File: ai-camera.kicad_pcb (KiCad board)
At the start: 4 copper layers, 70 x 70 mm, 161 parts, among them J1 Conn-01x02_P2mm_NONAME_JST-PH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, J2 USB_B_Micro_10118194-0001LF, J3 DBG, J4 Conn-02x10_P2.54mm_B-2100S20P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, J5 Conn-01x02_P1.25mm_10114829-1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, J6 Conn_01x24_FFC_0.5mm_hirose_F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, Q1 AO3401A, Q2 AO3400A, Q3 AO3400A, Q4 AO3401A, Q5 AO3400A, Q6 AO3401A, Q7 AO3400A, Q8 AO3400A, SW1 SW_PB_90deg_K2-1102AQ-H4CW-01, SW2 SW_PB_TS-1187A-B-A-B, SW3 SW_PB_TS-1187A-B-A-B, SW4 SW_PB_90deg_K2-1102AQ-H4CW-01, U1 SRV05-4, U10 AP1511B, U11 ESP32-S3-WROOM-1-N16R8, U12 MT9284-28J, U13 APDS-9306-065, U2 TP4057-42-SOT26-R, U3 PCF8563T/5,518, U4 XC6206-2.8V, U5 PIR_BS612, U6 SY8089AAAC, U7 SOT-23-6_SN74LVC1G373DBVR_TI, U8 XC6206-2.8V, U9 RT9166-12GVL, Y1 32.768kHz_Q13FC1350000400

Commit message: EAC-2: begin layout: low impedance ground connections, move DC-DC farther away, USB-C to prevent dips
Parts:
- removed the C29 at (136.8, 80.4)
- removed the C34 at (143.4, 73.1)
- removed the C35 at (141.8, 73.1)
- removed the D1 at (102.8, 87.7)
- removed the D2 at (102.8, 90.1)
- removed the R14 at (103.5, 67.1)
- removed the R17 at (108.3, 67.2)
- removed the R30 at (114.3, 85.7)
- removed RV1, RV2: 1M_3362P-1-105, 00-kiml-potentiometer-tht:Potentiometer_Vishay_T73YP_Vertical
- removed the TP29 at (104.6, 88.7)
- removed the U5 at (105.0, 59.0)
- added C11: 100u_CASE-B-3528_TAJB107K006RNJ, 00-kiml-capacitor-tantalum:CP_EIA-3528-15_AVX-H, F.Cu at (116.7, 101.2)
- added C14: 1u_0603_CL10A105KB8NNNC, Capacitor_SMD:C_0603_1608Metric, F.Cu at (120.9, 103.2)
- added C15: 100n_0402_CL05B104KB54PNC, Capacitor_SMD:C_0402_1005Metric, F.Cu at (119.7, 103.8)
- added C18: 100n_0402_CL05B104KB54PNC, Capacitor_SMD:C_0402_1005Metric, F.Cu at (119.7, 106.2)
- added C19: 10u_0603_CL10A106KP8NNNC, Capacitor_SMD:C_0603_1608Metric, F.Cu at (120.9, 106.8)
- added C21: 10u_0603_CL10A106KP8NNNC, Capacitor_SMD:C_0603_1608Metric, F.Cu at (124.0, 106.8)
- added C25: 10u_0603_CL10A106KP8NNNC, Capacitor_SMD:C_0603_1608Metric, F.Cu at (125.6, 106.8)
- added C27: 10u_0603_CL10A106KP8NNNC, Capacitor_SMD:C_0603_1608Metric, B.Cu at (119.3, 90.4)
- added C3: 1u_0603_CL10A105KB8NNNC, Capacitor_SMD:C_0603_1608Metric, F.Cu at (104.8, 87.0)
- added C31: 10u_0603_CL10A106KP8NNNC, Capacitor_SMD:C_0603_1608Metric, B.Cu at (126.7, 93.7)
- added C37: 100u_CASE-B-3528_TAJB107K006RNJ, 00-kiml-capacitor-tantalum:CP_EIA-3528-15_AVX-H, B.Cu at (152.8, 104.2)
- added C38: 100u_CASE-B-3528_TAJB107K006RNJ, 00-kiml-capacitor-tantalum:CP_EIA-3528-15_AVX-H, B.Cu at (152.8, 107.6)
- added C39: 100u_CASE-B-3528_TAJB107K006RNJ, 00-kiml-capacitor-tantalum:CP_EIA-3528-15_AVX-H, B.Cu at (152.8, 111.0)
- added C42: 1u_0603_CL10A105KB8NNNC, Capacitor_SMD:C_0603_1608Metric, F.Cu at (216.0, 116.3)
- added C43: 1u_0603_CL10A105KB8NNNC, Capacitor_SMD:C_0603_1608Metric, B.Cu at (156.9, 103.3)
- added C49: 1u_0603_CL10A105KB8NNNC, Capacitor_SMD:C_0603_1608Metric, F.Cu at (216.0, 118.8)
- added C50: 1u_0603_CL10A105KB8NNNC, Capacitor_SMD:C_0603_1608Metric, F.Cu at (216.0, 121.4)
- added C51: 1u_0603_CL10A105KB8NNNC, Capacitor_SMD:C_0603_1608Metric, F.Cu at (216.0, 123.9)
- added D14: 0603_IR_850nm_E6C0603IRAC1UDA, LED_SMD:LED_0603_1608Metric, F.Cu at (212.0, 116.0)
- added D15: 0603_IR_850nm_E6C0603IRAC1UDA, LED_SMD:LED_0603_1608Metric, F.Cu at (212.0, 118.6)
- added L2: 0805_FB_220R@100MHz_BLM21PG221SN1D, Inductor_SMD:L_0805_2012Metric_Pad1.15x1.40mm_HandSolder, F.Cu at (122.0, 100.7)
- added L4: 0805_FB_220R@100MHz_BLM21PG221SN1D, Inductor_SMD:L_0805_2012Metric_Pad1.15x1.40mm_HandSolder, B.Cu at (117.5, 90.8)
- added Q8: AO3401A, Package_TO_SOT_SMD:SOT-23, F.Cu at (146.9, -2.54)
- added R20: 10k_0402_0402WGF1002TCE, Resistor_SMD:R_0402_1005Metric, F.Cu at (159.9, -13.8)
- added R32: 2.43R_0805_0805W8F243KT5E, Resistor_SMD:R_0805_2012Metric, F.Cu at (216.2, 113.6)
- added R6: 5.1k_0603_0603WAF5101T5E, Resistor_SMD:R_0603_1608Metric, F.Cu at (98.5, 77.5)
- added R7: 5.1k_0603_0603WAF5101T5E, Resistor_SMD:R_0603_1608Metric, F.Cu at (100.1, 77.5)
- added R8: 10k_0402_0402WGF1002TCE, Resistor_SMD:R_0402_1005Metric, F.Cu at (105.9, 79.4)
- added U7: PIR_AS312, 00-kiml-optical:AS312, F.Cu at (151.5, -11.8)
- C1: value 10u_0603_CL10A106MA8NRNC -> 100u_CASE-B-3528_TAJB107K006RNJ; footprint Capacitor_SMD:C_0603_1608Metric -> 00-kiml-capacitor-tantalum:CP_EIA-3528-15_AVX-H; moved to F.Cu
- C12: value 22u_0805_CL21A226MAQNNNE -> 100u_CASE-B-3528_TAJB107K006RNJ; footprint Capacitor_SMD:C_0805_2012Metric -> 00-kiml-capacitor-tantalum:CP_EIA-3528-15_AVX-H; moved to F.Cu
- C13, C9: value 22u_0805_CL21A226MAQNNNE -> 10u_0603_CL10A106KP8NNNC; footprint Capacitor_SMD:C_0805_2012Metric -> Capacitor_SMD:C_0603_1608Metric; moved to F.Cu
- C17: renamed from C11; moved to F.Cu
- C20: value 10u_0603_CL10A106MA8NRNC -> 10u_0603_CL10A106KP8NNNC; moved to F.Cu
- C23: renamed from C15; value 10u_0603_CL10A106MA8NRNC -> 10u_0603_CL10A106KP8NNNC
- C26: value 22u_0805_CL21A226MAQNNNE -> 10u_0603_CL10A106KP8NNNC; footprint Capacitor_SMD:C_0805_2012Metric -> Capacitor_SMD:C_0603_1608Metric
- C30: renamed from C19; value 10u_0603_CL10A106MA8NRNC -> 10u_0603_CL10A106KP8NNNC
- C33: renamed from C22; value 10u_0603_CL10A106MA8NRNC -> 10u_0603_CL10A106KP8NNNC
- C34: renamed from C23; value 10u_0603_CL10A106MA8NRNC -> 10u_0603_CL10A106KP8NNNC
- C35: renamed from C24; value 10u_0603_CL10A106MA8NRNC -> 10u_0603_CL10A106KP8NNNC
- C36: renamed from C25; value 22u_0805_CL21A226MAQNNNE -> 10u_0603_CL10A106KP8NNNC; footprint Capacitor_SMD:C_0805_2012Metric -> Capacitor_SMD:C_0603_1608Metric
- C4: renamed from C3; moved to F.Cu
- C40: renamed from C28; value 22u_0805_CL21A226MAQNNNE -> 10u_0603_CL10A106KP8NNNC; footprint Capacitor_SMD:C_0805_2012Metric -> Capacitor_SMD:C_0603_1608Metric
- C41: renamed from C27; value 10u_0603_CL10A106MA8NRNC -> 10u_0603_CL10A106KP8NNNC
- C47: renamed from C33; moved to B.Cu
- C5, C7: value 10u_0603_CL10A106MA8NRNC -> 10u_0603_CL10A106KP8NNNC
- C53: renamed from C38; value 10u_0603_CL10A106MA8NRNC -> 10u_0603_CL10A106KP8NNNC
- C54: renamed from C39; moved to F.Cu
- C55: renamed from C40; moved to F.Cu
- C56: renamed from C41; moved to F.Cu
- C6: renamed from C4; value 22u_0805_CL21A226MAQNNNE -> 10u_0603_CL10A106KP8NNNC; footprint Capacitor_SMD:C_0805_2012Metric -> Capacitor_SMD:C_0603_1608Metric; moved to F.Cu
- C8: renamed from C6; value 10u_0603_CL10A106MA8NRNC -> 10u_0603_CL10A106KP8NNNC
- D3: renamed from D5; moved to F.Cu
- J2: value USB_B_Micro_10118194-0001LF -> TYPE-C-31-M-12; footprint 00-kiml-connector-usb:USB_Micro-B_Amphenol_10118194_Horizontal -> Connector_USB:USB_C_Receptacle_HRO_TYPE-C-31-M-12
- J6: value Conn_01x24_FFC_0.5mm_hirose_FH12-24S-0.5SH -> Conn_01x24_FFC_0.5mm_AFC01-S24FCC-00; footprint 00-kiml-connector-fpc-ffc:Hirose_FH12-24S-0.5SH_1x24-1MP_P0.50mm_Horizontal -> 00-kiml-connector-fpc-ffc:Jushuo_AFC01-S24FCC-00_1x24-1MP_P0.50_Horizontal
- JP1, JP2, Q2, Q3, Q5, U2, U6, Y1: moved to F.Cu
- L3: renamed from L2; moved to F.Cu
- Q9: renamed from Q8; moved to F.Cu
- R10: renamed from R7; moved to F.Cu
- R11: renamed from R8; moved to F.Cu
- R12: renamed from R9; moved to F.Cu
- R17: renamed from R12; moved to F.Cu
- R21: renamed from R16; moved to F.Cu
- R22: renamed from R18; moved to F.Cu
- R23: renamed from R19; moved to F.Cu
- R24: renamed from R20; moved to F.Cu
- R25: renamed from R23; moved to F.Cu
- R26: renamed from R24; moved to F.Cu
- R4: renamed from R3; moved to F.Cu
- R5: renamed from R4; moved to F.Cu
- R9: renamed from R6; moved to F.Cu
- REF**: value ircut_filter_M12_30mm_noname -> ircut_filter_M12_10mm_noname; footprint 00-kiml-optical:ircut_filter_M12_30mm_noname -> 00-kiml-optical:ircut_filter_M12_10mm_noname
- U1: renamed from U3; moved to F.Cu
- moved C23 161.4 mm to (-3.25, 132.0)
- moved C24 153.9 mm to (-0.97, 113.4)
- moved TP28 134.3 mm to (232.0, 54.5)
- moved TP25 129.6 mm to (232.0, 43.8)
- moved TP29 128.5 mm to (232.0, 58.0)
- moved TP4 125.2 mm to (217.8, 54.5)
- moved TP24 124.6 mm to (228.4, 61.5)
- moved TP3 124.4 mm to (217.8, 50.9)
- moved TP22 123.9 mm to (228.4, 54.5)
- moved TP21 122.2 mm to (228.4, 50.9)
- moved TP23 121.9 mm to (228.4, 58.0)
- moved TP16 118.7 mm to (224.9, 54.5)
- moved D13 117.3 mm to (212.0, 113.5)
- moved TP26 116.0 mm to (232.0, 47.4)
- moved D11 115.3 mm to (212.0, 108.3)
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- renumbered C8 to C16, C14 to C22, C16 to C24, C17 to C28, C18 to C29, C21 to C32, C31 to C44, C30 to C45, C32 to C46, C36 to C48, C37 to C52, D3 to D1, D12 to D10, D13 to D11, D14 to D12, D15 to D13, D4 to D2, D6 to D4, D7 to D5, D8 to D6, D9 to D7, D10 to D8, D11 to D9, L3 to L5, R10 to R13, R11 to R14, R22 to R15, R21 to R16, R13 to R18, R15 to R19, R25 to R27, R26 to R28, R27 to R29, R5 to R3, R28 to R30, R29 to R31, TP30 to TP29, U4 to U3, U1 to U4, U7 to U5
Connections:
- C1 pad 1: GND -> +BATT
- C1 pad 2: Net-(C1-Pad2) -> GND
- C12 pad 1: +3V3 -> Net-(Q6-S)
- C13 pad 1: +3V3 -> GND
- C13 pad 2: GND -> Net-(Q6-S)
- C20 pad 1: +3V3 -> GND
- C20 pad 2: GND -> +3V3
- C30 pad 1: +3V3 -> +3.3VA
- C48 pad 1: GND -> Net-(D5-K)
- C48 pad 2: Net-(C35-Pad1) -> GND
- C53 pad 1: +3V3 -> +3.3VA
- C55 pad 2: +3V3 -> +3.3VA
- C9 pad 1: VBUS -> GND
- C9 pad 2: GND -> VBUS
- D12 pad 1: Net-(D14-Pad1) -> Net-(D12-K)
- D13 pad 2: Net-(D14-Pad1) -> Net-(D13-A)
- D5 pad 1: Net-(C35-Pad1) -> Net-(D5-K)
- D6 pad 2: Net-(C35-Pad1) -> Net-(D5-K)
- J3 pad 1: +5P -> +5V
- J6 pad 14: +3V3 -> +3.3VA
- JP1 pad 2: Net-(C1-Pad2) -> +5V
- L1 pad 1: Net-(J2-Pad1) -> Net-(J2-VBUS-PadA4)
- L1 pad 2: +5F -> +5V
- Q6 pad 2: VBUS -> Net-(Q6-S)
- R18 pad 1: VBUS -> Net-(Q6-S)
- R4 pad 1: Net-(C1-Pad2) -> +5V
- R5 pad 1: Net-(C1-Pad2) -> +5V
- TP28 pad 1: +5F -> +5V
- U12 pad 5: Net-(C35-Pad1) -> Net-(D5-K)
- U2 pad 4: Net-(C1-Pad2) -> +5V
- U4 pad 5: Net-(J2-Pad1) -> +5V
- U6 pad 4: VBUS -> Net-(Q6-S)
- U8 pad 3: +3V3 -> +3.3VA
- U9 pad 3: +3V3 -> +3.3VA
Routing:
- net +3V3: track 306.5 -> 99.0 mm, vias 17 -> 9
- net VBUS: track 208.5 -> 71.1 mm, vias 6 -> 8
- net /ESP_BOOT: track 157.3 -> 26.2 mm, vias 4 -> 1
- net GND: track 119.8 -> 31.5 mm, vias 151 -> 88
- net /ESP_EN: track 129.8 -> 44.0 mm, vias 5 -> 1
- net /BATT_DETECT: track 84.5 -> 0.00 mm, vias 3 -> 0
- net /RXD0: track 102.8 -> 20.3 mm, vias 3 -> 1
- net /TXD0: track 104.3 -> 25.7 mm, vias 3 -> 1
- net /CAM.SDA: track 131.6 -> 55.2 mm, vias 5 -> 3
- net /PIR_CTRL_D: track 72.0 -> 0.00 mm, vias 1 -> 0
- net /PIR_CTRL_LE: track 52.8 -> 0.00 mm, vias 1 -> 0
- net Net-(D11-K): track 51.0 -> 0.00 mm
- net /USR_BTN: track 47.4 -> 0.00 mm, vias 2 -> 0
- net /IRCUT_CTRL: track 46.9 -> 0.00 mm, vias 3 -> 0
- net Net-(Q5-D): track 121.4 -> 78.8 mm, vias 4 -> 2
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- added copper zone on F.Cu, net +3V3
- added copper zone on B.Cu, net +5V
- added copper zone on F.Cu, net +5V
- added copper zone on F.Cu, net +BATT
- added copper zone on F.Cu, net GND
- added copper zone on F.Cu, net Net-(Q6-S)
- added copper zone on F.Cu, net VBUS
- removed copper zone on B.Cu, net +5F
- removed copper zone on F.Cu, net +5F
- removed copper zone on B.Cu, net Net-(C1-Pad2)
- removed copper zone on F.Cu, net Net-(J2-Pad1)
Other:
- board text removed: "+BATT"
- board text removed: "IRCUT"
- board text removed: "O1"
- board text removed: "O2"
- board text removed: "ONTIME"
- board text removed: "SENS"
- board text removed: "USR"
- board text removed: "~{CHRG}"
- board text removed: "~{STDBY}"

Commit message: EAC-2: prelim layout done
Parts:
- removed TP1, TP10, TP11, TP12, TP13, TP14, TP15, TP16, TP17, TP18, TP19, TP2, TP20, TP21, TP22, TP23, TP24, TP25, TP26, TP27, TP28, TP29, TP3, TP4, TP5, TP6, TP7, TP8, TP9: TP, TestPoint:TestPoint_Pad_D1.5mm
- added C57: 100n_0402_CL05B104KB54PNC, Capacitor_SMD:C_0402_1005Metric, B.Cu at (155.8, 79.9)
- C22, JP2, Q5, Q8, Q9, R17, R20, R22: moved to B.Cu
- C23, C40, C44, C48, D5, L5, R31, U12: moved to F.Cu
- moved C23 160.6 mm to (154.4, 101.4)
- moved C24 153.8 mm to (149.1, 79.8)
- moved R31 129.3 mm to (99.0, 66.6), turned to 0 degrees
- moved D5 125.6 mm to (104.6, 70.6), turned to 180 degrees
- moved C44 123.8 mm to (102.6, 74.4), turned to -90 degrees
- moved C50 123.2 mm to (105.4, 67.1)
- moved U12 123.1 mm to (100.1, 68.9), turned to 180 degrees
- moved C48 122.6 mm to (107.5, 70.4)
- moved C49 121.5 mm to (105.4, 68.6)
- moved C40 121.1 mm to (103.9, 73.8), turned to -90 degrees
- moved C51 120.9 mm to (108.5, 68.6), turned to 180 degrees
- moved L5 119.7 mm to (99.8, 73.0)
- moved C42 118.5 mm to (105.5, 73.8), turned to 90 degrees
- moved D10 112.7 mm to (115.0, 55.0)
- moved SW4 109.6 mm to (136.0, 49.5)
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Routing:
- net /BATT_DETECT: track 0.00 -> 124.9 mm
- net /IRLED_PWM: track 0.00 -> 81.9 mm, vias 0 -> 4
- net Net-(Q5-D): track 78.8 -> 149.0 mm, vias 2 -> 4
- net /ESP_BOOT: track 26.2 -> 82.9 mm
- net /PIR_CTRL_D: track 0.00 -> 55.8 mm, vias 0 -> 2
- net /PIR_CTRL_LE: track 0.00 -> 53.8 mm, vias 0 -> 2
- net /CAM.SDA: track 55.2 -> 103.1 mm
- net /CAM.SCL: track 65.3 -> 108.3 mm
- net /USR_BTN: track 0.00 -> 40.9 mm, vias 0 -> 2
- net Net-(D10-K): track 0.00 -> 39.8 mm
- net Net-(D11-K): track 0.00 -> 39.0 mm
- net /PIR_OUT: track 0.00 -> 38.8 mm, vias 0 -> 2
- net /IRCUT_CTRL: track 0.00 -> 38.6 mm, vias 0 -> 2
- net GND: track 31.5 -> 61.2 mm, vias 88 -> 127
- net +BATT: track 37.5 -> 63.0 mm
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
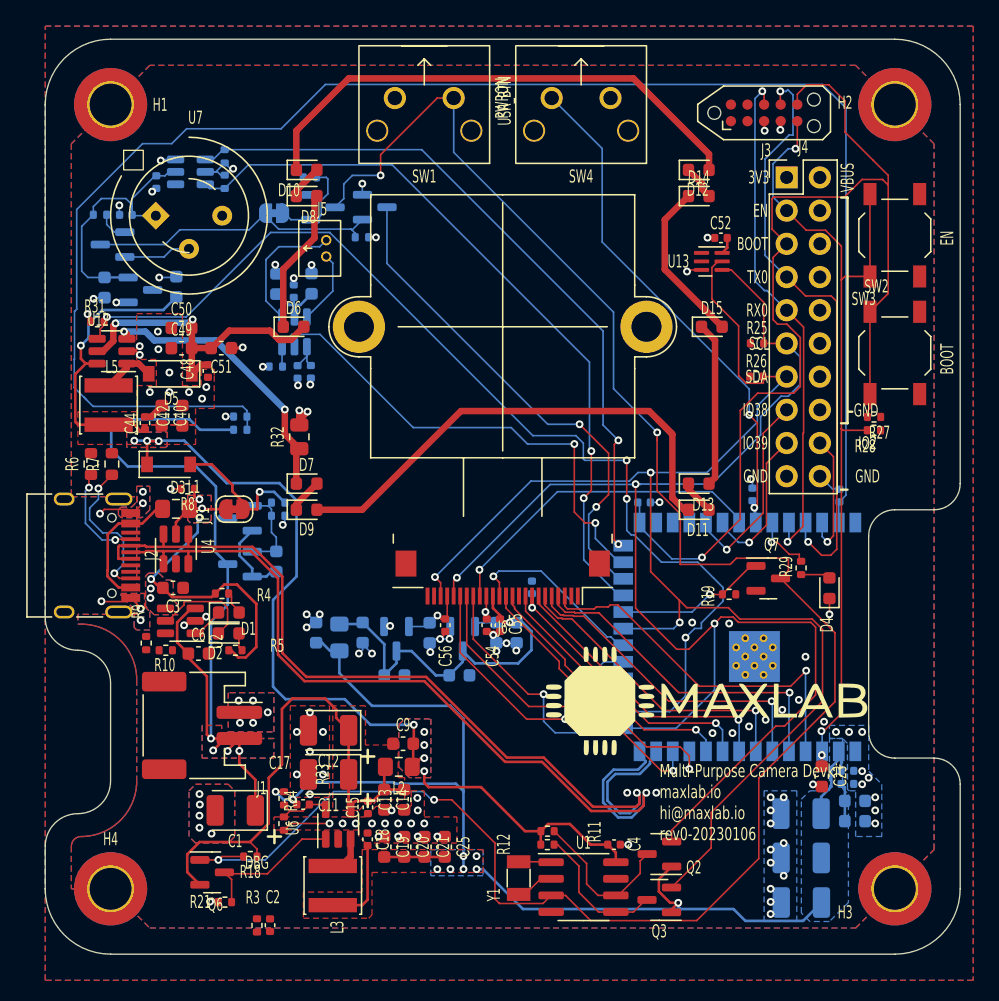
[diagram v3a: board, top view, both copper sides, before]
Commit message: EAC-2: test points and DRC error fixes
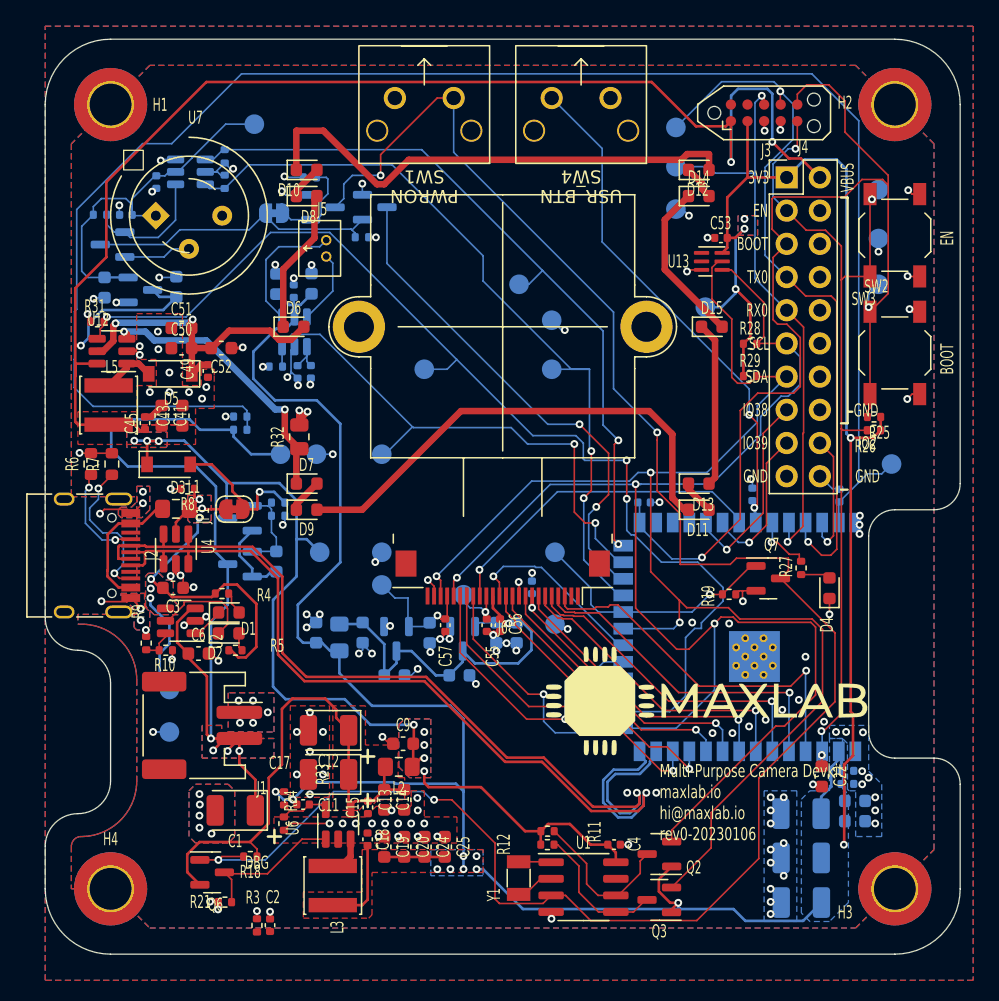
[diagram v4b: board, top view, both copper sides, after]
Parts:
- added TP1: TP, TestPoint:TestPoint_Pad_D1.5mm, B.Cu at (158.8, 56.5)
- added TP10: TP, TestPoint:TestPoint_Pad_D1.5mm, B.Cu at (120.8, 76.8)
- added TP11: TP, TestPoint:TestPoint_Pad_D1.5mm, B.Cu at (159.8, 77.5)
- added TP12: TP, TestPoint:TestPoint_Pad_D1.5mm, B.Cu at (134.0, 84.2)
- added TP13: TP, TestPoint:TestPoint_Pad_D1.5mm, B.Cu at (111.0, 51.5)
- added TP14: TP, TestPoint:TestPoint_Pad_D1.5mm, B.Cu at (124.0, 70.2)
- added TP15: TP, TestPoint:TestPoint_Pad_D1.5mm, B.Cu at (134.0, 89.8)
- added TP16: TP, TestPoint:TestPoint_Pad_D1.5mm, B.Cu at (127.0, 87.5)
- added TP17: TP, TestPoint:TestPoint_Pad_D1.5mm, B.Cu at (120.8, 84.2)
- added TP18: TP, TestPoint:TestPoint_Pad_D1.5mm, B.Cu at (120.8, 86.8)
- added TP19: TP, TestPoint:TestPoint_Pad_D1.5mm, B.Cu at (113.0, 76.8)
- added TP2: TP, TestPoint:TestPoint_Pad_D1.5mm, B.Cu at (158.8, 63.8)
- added TP20: TP, TestPoint:TestPoint_Pad_D1.5mm, B.Cu at (115.8, 76.8)
- added TP21: TP, TestPoint:TestPoint_Pad_D1.5mm, B.Cu at (116.0, 84.2)
- added TP22: TP, TestPoint:TestPoint_Pad_D1.5mm, B.Cu at (145.5, 65.5)
- added TP23: TP, TestPoint:TestPoint_Pad_D1.5mm, B.Cu at (104.5, 94.8)
- added TP24: TP, TestPoint:TestPoint_Pad_D1.5mm, B.Cu at (104.5, 98.0)
- added TP3: TP, TestPoint:TestPoint_Pad_D1.5mm, B.Cu at (158.8, 60.2)
- added TP4: TP, TestPoint:TestPoint_Pad_D1.5mm, B.Cu at (143.2, 51.8)
- added TP5: TP, TestPoint:TestPoint_Pad_D1.5mm, B.Cu at (143.2, 54.8)
- added TP6: TP, TestPoint:TestPoint_Pad_D1.5mm, B.Cu at (143.2, 58.0)
- added TP7: TP, TestPoint:TestPoint_Pad_D1.5mm, B.Cu at (131.2, 63.8)
- added TP8: TP, TestPoint:TestPoint_Pad_D1.5mm, B.Cu at (133.8, 70.2)
- added TP9: TP, TestPoint:TestPoint_Pad_D1.5mm, B.Cu at (133.8, 66.5)
- moved R28 0.53 mm to (148.9, 68.3)
- moved R29 0.48 mm to (148.9, 70.8)
- renumbered C22 to C21, C23 to C22, C24 to C23, C21 to C24, C57 to C32, C32 to C33, C33 to C34, C34 to C35, C35 to C36, C36 to C37, C37 to C38, C38 to C39, C39 to C40, C40 to C41, C41 to C42, C42 to C43, C43 to C44, C44 to C45, C45 to C46, C46 to C47, C47 to C48, C48 to C49, C49 to C50, C50 to C51, C51 to C52, C52 to C53, C53 to C54, C54 to C55, C55 to C56, C56 to C57, R27 to R25, R28 to R26, R29 to R27, R25 to R28, R26 to R29
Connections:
- J3 pad 1: +5V -> VBUS
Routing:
- net +3V3: track 103.6 -> 227.8 mm, vias 9 -> 14
- net VBUS: track 90.4 -> 185.2 mm, vias 9 -> 11
- net GND: track 61.2 -> 99.0 mm, vias 127 -> 162
- net /TXD0: track 45.8 -> 55.0 mm
- net +5V: track 29.9 -> 38.2 mm
- net /PWR_EN: track 11.2 -> 19.1 mm
- net /PWR_PIR: track 21.6 -> 29.0 mm
- net Net-(Q8-G): track 2.37 -> 9.72 mm
- net /RXD0: track 39.5 -> 44.9 mm
- net +BATT: track 63.0 -> 67.7 mm
- net +2V8: track 4.44 -> 8.97 mm
- net /BATT_DETECT: track 124.9 -> 129.1 mm
- net /PIR_CTRL_D: track 55.8 -> 59.5 mm
- net /IRCUT_CTRL: track 38.6 -> 41.5 mm
- net Net-(U2-PROG): track 0.00 -> 2.45 mm
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
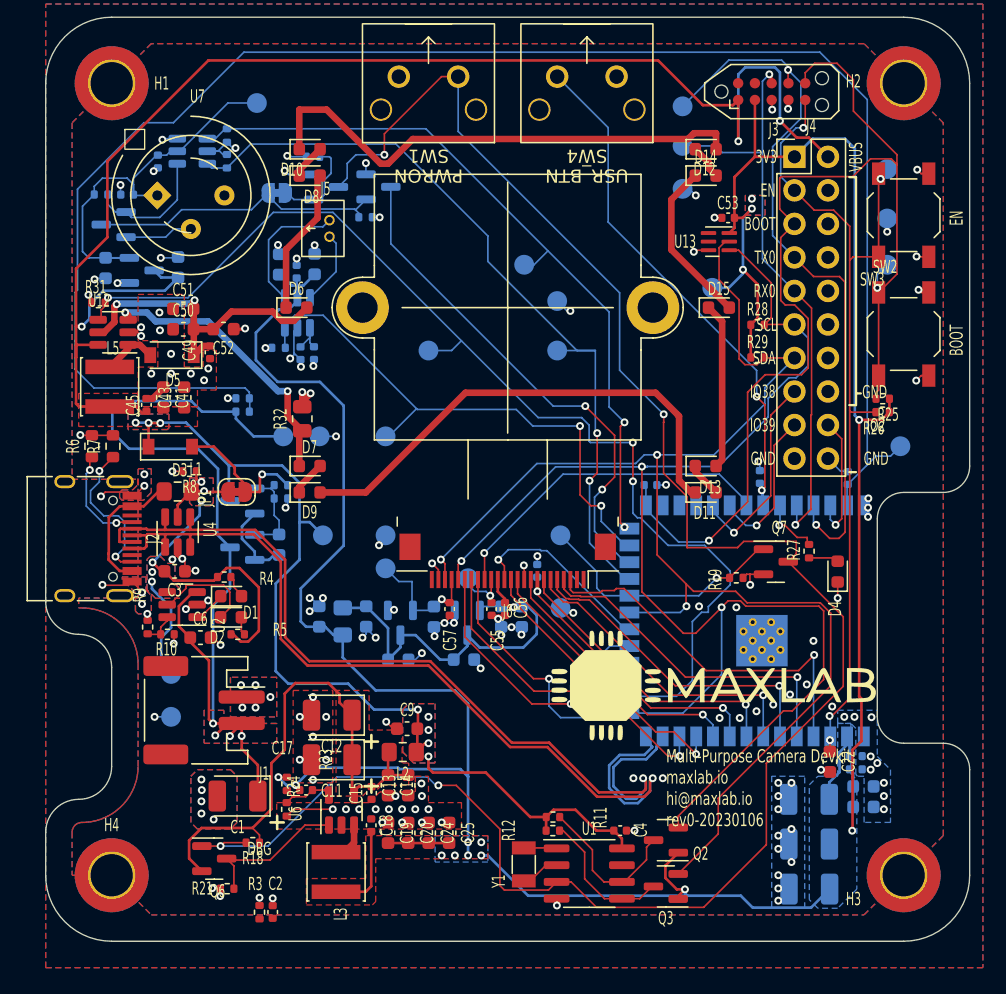
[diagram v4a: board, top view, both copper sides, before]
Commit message: EAC-2: top silkscreen fix
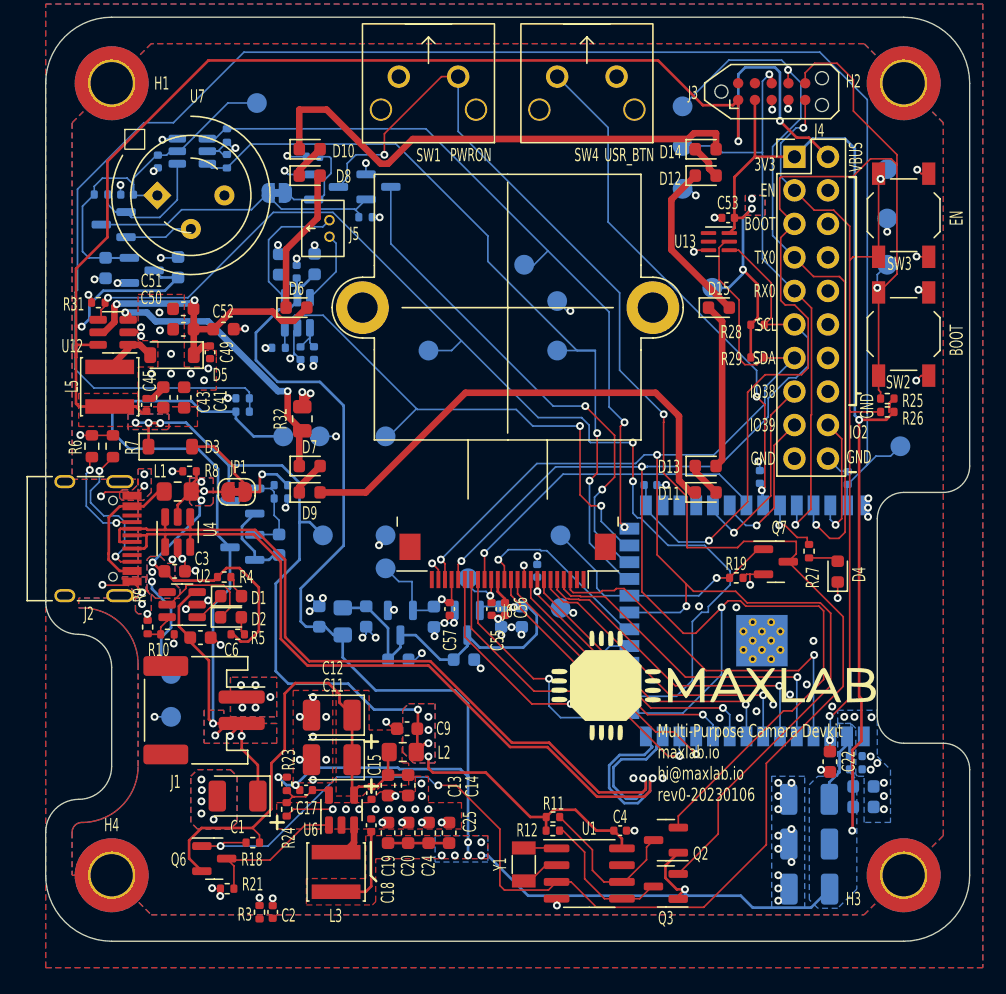
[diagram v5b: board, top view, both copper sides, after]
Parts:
- moved R26 0.36 mm to (158.8, 74.9)
- moved R25 0.35 mm to (158.8, 73.9)
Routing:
- net +3V3: track 227.8 -> 228.3 mm
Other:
- board text removed: "DBG"
